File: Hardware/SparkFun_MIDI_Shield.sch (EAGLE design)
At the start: 34 parts, among them J1 MIDI IN, J2 MIDI OUT, J3 UNO_R3_SHIELD, U1 6N138M, U2 74AHC1G125

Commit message: Prototype Revisions WIP
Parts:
- J1, J2: device Testing:5-PIN-CIRCULAR-DINFULL_SIZE -> Testing:5-PIN-CIRCULAR-DINNEW
- J3: device Testing:ARDUINO_R3_SHIELDUNO_R3_SHIELD_HOLES -> SparkFun-Boards:ARDUINO_R3_SHIELD
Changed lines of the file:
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@@
 <layer number="113" name="IDFDebug" color="4" fill="1" visible="yes" active="yes"/>
 <layer number="116" name="Patch_BOT" color="9" fill="4" visible="yes" active="yes"/>
+<layer number="118" name="Rect_Pads" color="7" fill="1" visible="yes" active="yes"/>
 <layer number="121" name="_tsilk" color="7" fill="1" visible="yes" active="yes"/>
 <layer number="122" name="_bsilk" color="7" fill="1" visible="yes" active="yes"/>
@@
 <part name="S4" library="SparkFun-Electromechanical" deviceset="SWITCH-MOMENTARY-2" device="12MM"/>
 <part name="S5" library="SparkFun-Electromechanical" deviceset="SWITCH-MOMENTARY-2" device="12MM"/>
-<part name="J1" library="Testing" deviceset="5-PIN-CIRCULAR-DIN" device="FULL_SIZE" value="MIDI IN"/>
-<part name="J2" library="Testing" deviceset="5-PIN-CIRCULAR-DIN" device="FULL_SIZE" value="MIDI OUT"/>
+<part name="J1" library="Testing" deviceset="5-PIN-CIRCULAR-DIN" device="NEW" value="MIDI IN"/>
+<part name="J2" library="Testing" deviceset="5-PIN-CIRCULAR-DIN" device="NEW" value="MIDI OUT"/>
 <part name="GND7" library="SparkFun" deviceset="GND" device=""/>
 <part name="FRAME1" library="SparkFun-Aesthetics" deviceset="FRAME-LETTER" device="" value="Frame"/>
 <part name="RV1" library="SparkFun-Electromechanical" deviceset="POT" device="" value="10k"/>
 <part name="RV2" library="SparkFun-Electromechanical" deviceset="POT" device="" value="10k"/>
-<part name="J3" library="Testing" deviceset="ARDUINO_R3_SHIELD" device="UNO_R3_SHIELD_HOLES" value="UNO_R3_SHIELD"/>
+<part name="J3" library="SparkFun-Boards" deviceset="ARDUINO_R3_SHIELD" device="" value="UNO_R3_SHIELD"/>
 <part name="U2" library="SparkFun-DigitalIC" deviceset="74AHC1G125" device=""/>
 <part name="P+5" library="SparkFun" deviceset="VCC" device=""/>

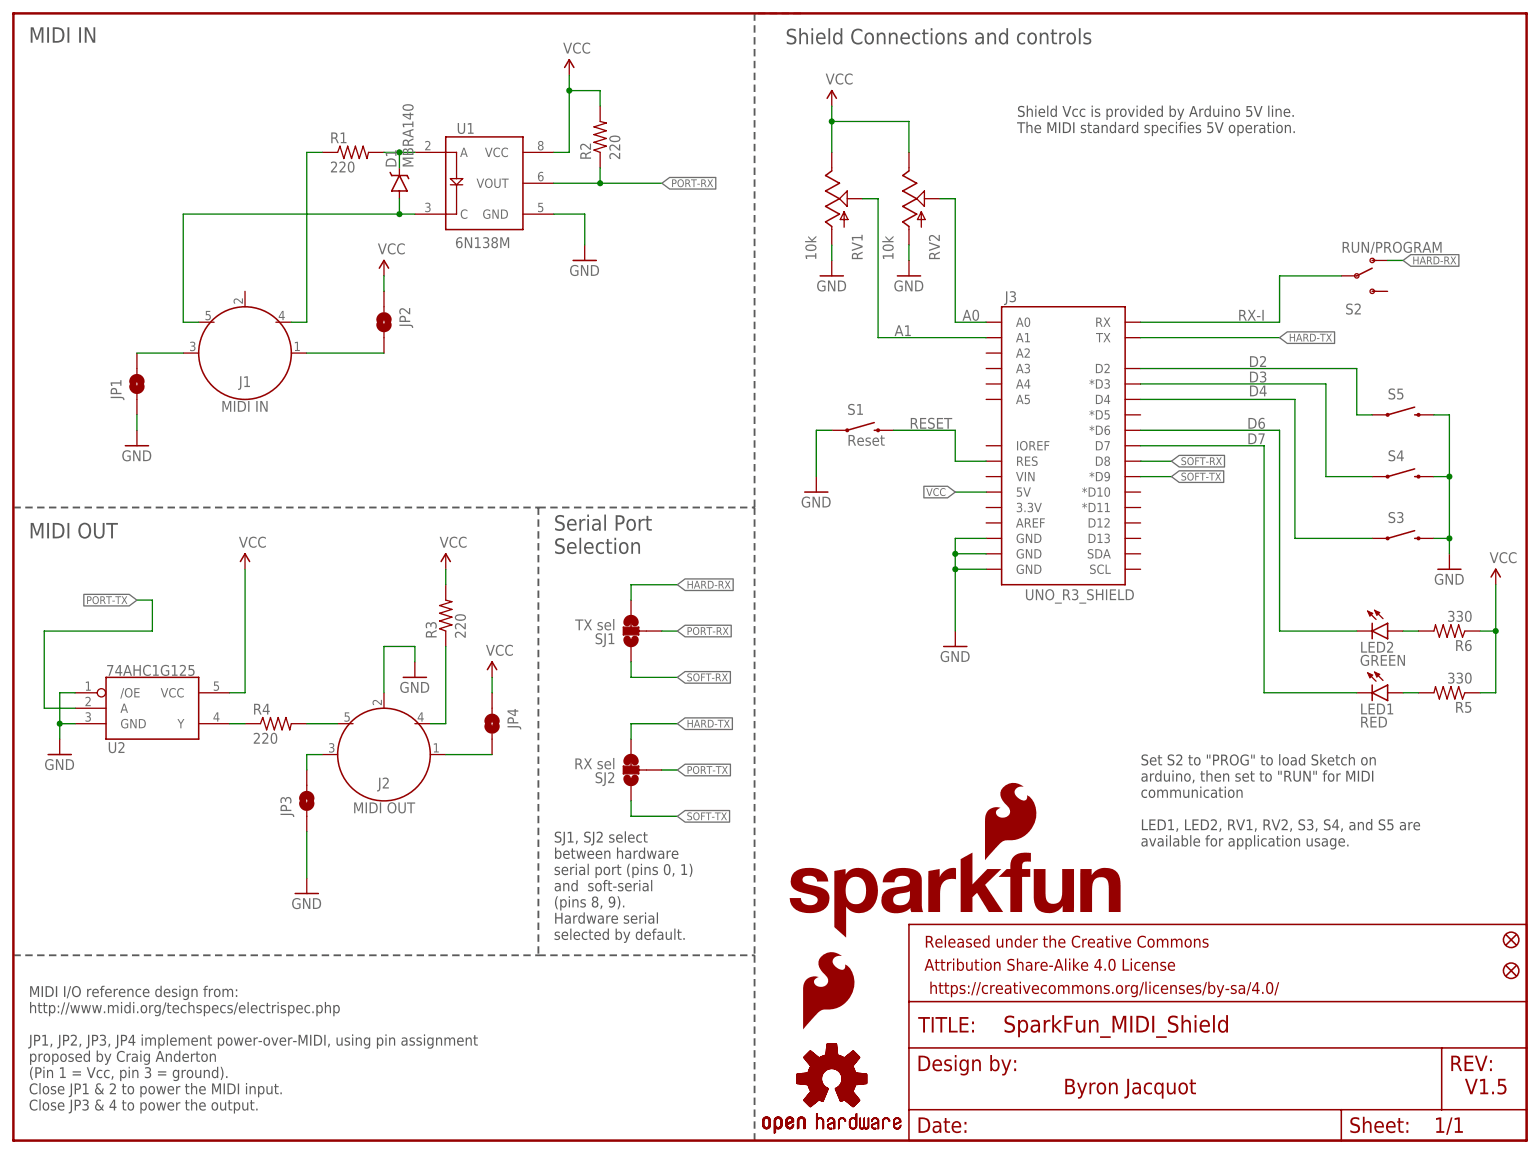
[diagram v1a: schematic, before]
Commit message: WIP Mostly complete.
Proto issues handles.
-Pots turn the right way.
-Option for out vs thru.
-JP/SJ terminology resolved.
-More clearance around new connector component.
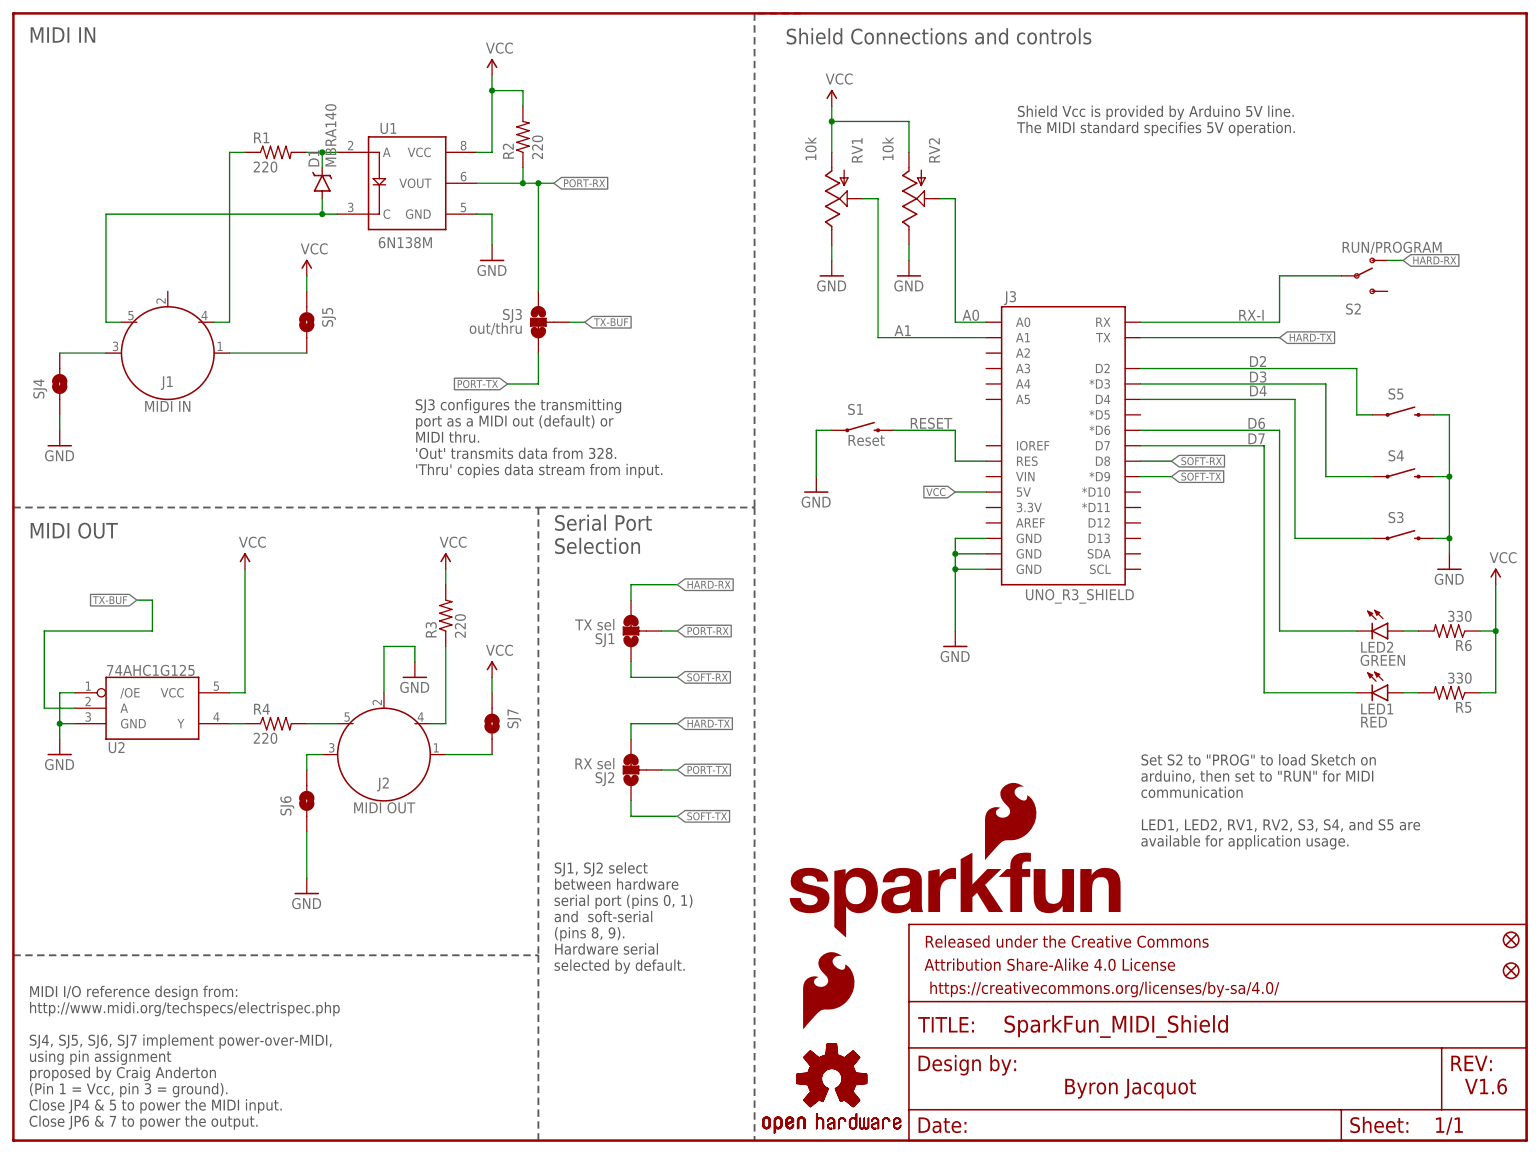
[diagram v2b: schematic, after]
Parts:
- removed JP1, JP2: JUMPER-PAD-2-NOYES_SILK, SparkFun-Passives:JUMPER-PAD-2-NOYES_SILK
- added SJ3: out/thru, SparkFun-Passives:JUMPER-PAD-3-2OF3_NC_BY_TRACE_SMALL
- added SJ4, SJ5: JUMPER-PAD-2-NOYES_SILK, SparkFun-Passives:JUMPER-PAD-2-NOYES_SILK
- renumbered JP3 to SJ6, JP4 to SJ7
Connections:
- new net TX-BUF: SJ3.2, U2.A
- net GND: now also RV1.E, RV2.E, SJ4.1; no longer JP1.1, RV1.A, RV2.A
- net N$6: now also SJ4.2; no longer JP1.2
- net N$7: now also SJ5.2; no longer JP2.2
- net PORT-RX: now also SJ3.1
- net PORT-TX: now also SJ3.3; no longer U2.A
- net VCC: now also RV1.A, RV2.A, SJ5.1; no longer JP2.1, RV1.E, RV2.E
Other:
- note added: "MIDI I/O reference design from: http://www.midi.org/techspecs/electrispec.php SJ4, SJ5, SJ6, SJ7 implement power-over-MIDI, using pin assignment proposed by Craig Anderton (Pin 1 = Vcc, pin 3 = ground). Close JP4 & 5 to power the MIDI input. Close JP6 & 7 to power the output."
- note added: "SJ3 configures the transmitting port as a MIDI out (default) or MIDI thru. 'Out' transmits data from 328. 'Thru' copies data stream from input."
- note added: "V1.6"
- note removed: "MIDI I/O reference design from: http://www.midi.org/techspecs/electrispec.php JP1, JP2, JP3, JP4 implement power-over-MIDI, using pin assignment proposed by Craig Anderton (Pin 1 = Vcc, pin 3 = ground). Close JP1 & 2 to power the MIDI input. Close JP3 & 4 to power the output."
- note removed: "V1.5"
- moved on the sheet: D1, J1, R1, R2, RV1, RV2, U1

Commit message: Board updates.
Small tweaks before submission for review.
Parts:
- added U$1: REVISION, SparkFun-Aesthetics:REVISION
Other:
- note added: "Chris Taylor"
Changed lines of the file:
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@@
 <part name="U1" library="SparkFun-DiscreteSemi" deviceset="OPTO_DARL_6N138S" device="" value="6N138M"/>
 <part name="SJ3" library="SparkFun-Passives" deviceset="JUMPER-PAD-3-2OF3_NC_BY_TRACE" device="_SMALL" value="out/thru"/>
+<part name="U$1" library="SparkFun-Aesthetics" deviceset="REVISION" device=""/>
 </parts>
 <sheets>
@@
 <text x="2.54" y="180.594" size="2.54" layer="97">MIDI IN</text>
 <text x="2.54" y="99.06" size="2.54" layer="97">MIDI OUT</text>
-<text x="172.72" y="7.62" size="2.54" layer="94">Byron Jacquot</text>
+<text x="175.006" y="6.604" size="2.54" layer="94">Byron Jacquot</text>
 <text x="238.76" y="7.62" size="2.54" layer="94">V1.6</text>
 <wire x1="129.54" y1="185.42" x2="121.92" y2="185.42" width="0.3048" layer="94" style="shortdash"/>
@@
 'Thru' copies data stream from input.
 </text>
+<text x="170.434" y="11.176" size="2.54" layer="94">Chris Taylor</text>
 </plain>
 <instances>
@@
 <instance part="U1" gate="G$1" x="63.5" y="160.02"/>
 <instance part="SJ3" gate="G$1" x="86.36" y="134.62" rot="MR0"/>
+<instance part="U$1" gate="G$1" x="148.844" y="6.858"/>
 </instances>
 <busses>

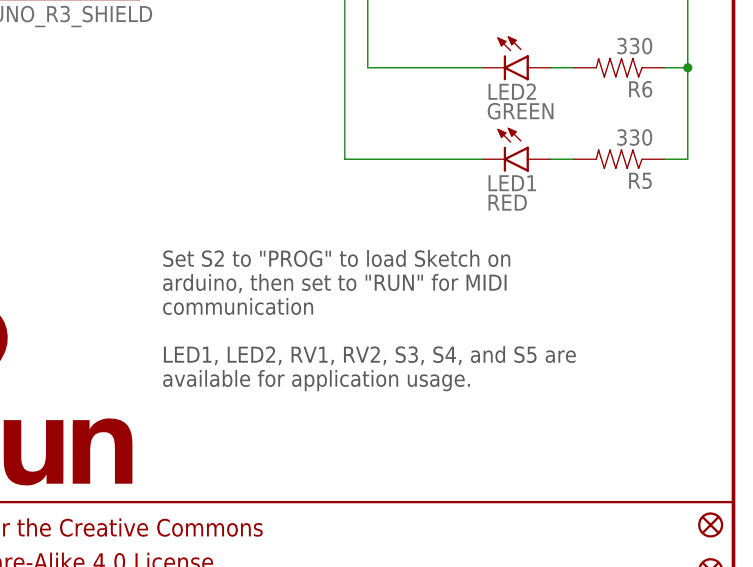
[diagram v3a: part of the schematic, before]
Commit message: Small text change
Fixing capitalization...really a change to get my renamed branch pushed
(V_1.5 -> V_1.6).
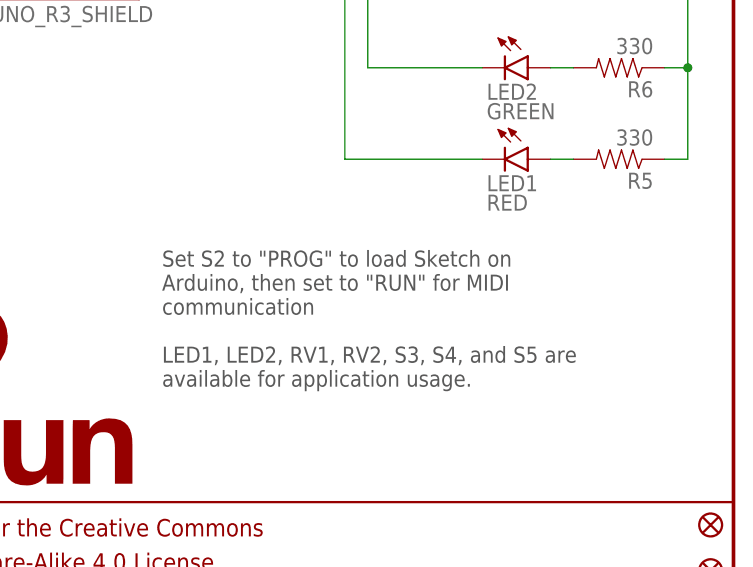
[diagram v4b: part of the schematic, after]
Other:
- note added: "Set S2 to "PROG" to load Sketch on Arduino, then set to "RUN" for MIDI communication LED1, LED2, RV1, RV2, S3, S4, and S5 are available for application usage."
- note removed: "Set S2 to "PROG" to load Sketch on arduino, then set to "RUN" for MIDI communication LED1, LED2, RV1, RV2, S3, S4, and S5 are available for application usage."
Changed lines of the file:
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@@
 Close JP6 &amp; 7 to power the output.</text>
 <text x="185.42" y="63.5" size="1.778" layer="97" align="top-left">Set S2 to "PROG" to load Sketch on
-arduino, then set to "RUN" for MIDI
+Arduino, then set to "RUN" for MIDI
 communication
 LED1, LED2, RV1, RV2, S3, S4, and S5 are
